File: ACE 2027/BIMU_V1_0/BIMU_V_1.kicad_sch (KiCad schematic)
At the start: 0 parts

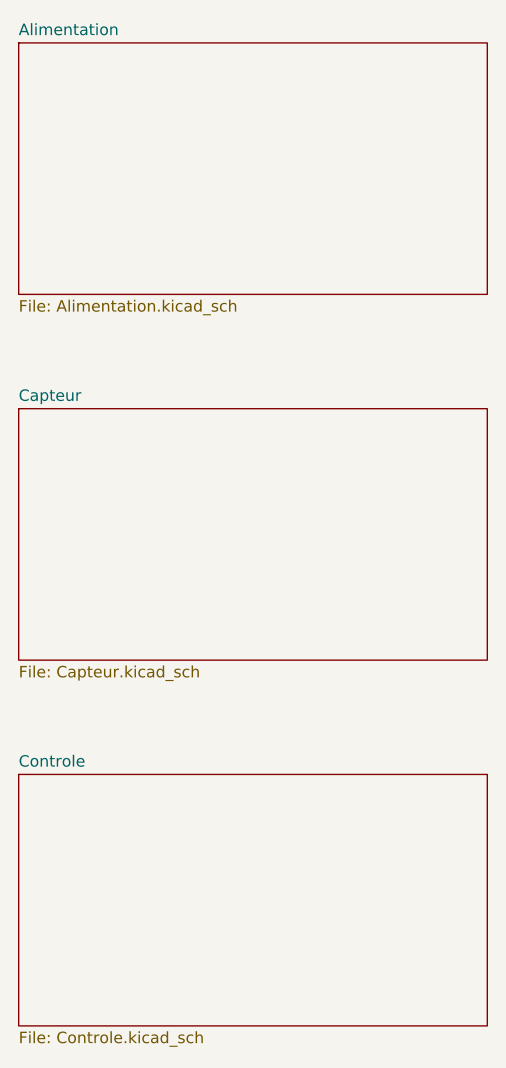
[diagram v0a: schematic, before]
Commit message: Avancement of different part of the schematic
Add and reorganize numerous symbol definitions and annotations in Alimentation.kicad_sch: new TestPoint, LED, R_US/Resistor symbols, BAV99 diode, MountingHole, AP7361C-33E regulator, power/GND symbol instances, and associated symbol variants. Add global CAN_P/CAN_N labels, layout rectangles and text (ESD protection, current rating), and adjust wires/junction coordinates. Also update BIMU_V_1.kicad_pcb, BIMU_V_1.kicad_sch, Capteur.kicad_sch, Controle.kicad_sch and fp-info-cache; add several backup .zip files and a Controle.kicad_sch-bak file.
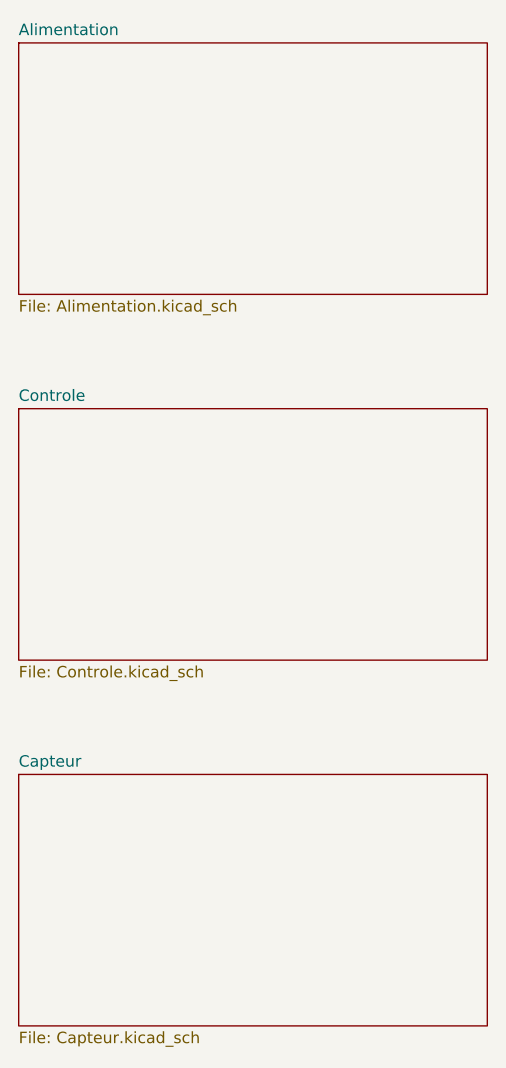
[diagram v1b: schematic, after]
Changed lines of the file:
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@@
 		)
 		(instances
-			(project "BIMU"
+			(project "BIMU_V_1"
 				(path "/abeb93ed-b9ef-4503-99a7-3fce380ff294"
 					(page "1")
+				)
+			)
+		)
+	)
+	(sheet
+		(at 17.78 58.42)
+		(size 52.07 27.94)
+		(exclude_from_sim no)
+		(in_bom yes)
+		(on_board yes)
+		(dnp no)
+		(fields_autoplaced yes)
+		(stroke
+			(width 0.1524)
+			(type solid)
+		)
+		(fill
+			(color 0 0 0 0.0000)
+		)
+		(property "Sheetname" "Controle"
+			(at 17.78 57.7084 0)
+			(effects
+				(font
+					(size 1.27 1.27)
+				)
+				(justify left bottom)
+			)
+		)
+		(property "Sheetfile" "Controle.kicad_sch"
+			(at 17.78 86.9446 0)
+			(effects
+				(font
+					(size 1.27 1.27)
+				)
+				(justify left top)
+			)
+		)
+		(instances
+			(project "BIMU_V_1"
+				(path "/abeb93ed-b9ef-4503-99a7-3fce380ff294"
+					(page "2")
 				)
 			)
@@
 			(color 0 0 0 0.0000)
 		)
-		(property "Sheetname" "Controle"
+		(property "Sheetname" "Capteur"
 			(at 17.78 98.3484 0)
 			(effects
@@
 			)
 		)
-		(property "Sheetfile" "Controle.kicad_sch"
+		(property "Sheetfile" "Capteur.kicad_sch"
 			(at 17.78 127.5846 0)
 			(effects
@@
 		)
 		(instances
-			(project "BIMU"
-				(path "/abeb93ed-b9ef-4503-99a7-3fce380ff294"
-					(page "2")
-				)
-			)
-		)
-	)
-	(sheet
-		(at 17.78 58.42)
-		(size 52.07 27.94)
-		(exclude_from_sim no)
-		(in_bom yes)
-		(on_board yes)
-		(dnp no)
-		(fields_autoplaced yes)
-		(stroke
-			(width 0.1524)
-			(type solid)
-		)
-		(fill
-			(color 0 0 0 0.0000)
-		)
-		(property "Sheetname" "Capteur"
-			(at 17.78 57.7084 0)
-			(effects
-				(font
-					(size 1.27 1.27)
-				)
-				(justify left bottom)
-			)
-		)
-		(property "Sheetfile" "Capteur.kicad_sch"
-			(at 17.78 86.9446 0)
-			(effects
-				(font
-					(size 1.27 1.27)
-				)
-				(justify left top)
-			)
-		)
-		(instances
-			(project "BIMU"
+			(project "BIMU_V_1"
 				(path "/abeb93ed-b9ef-4503-99a7-3fce380ff294"
 					(page "3")
